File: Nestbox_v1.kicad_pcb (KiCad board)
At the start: 2 copper layers, 78 parts, among them P1 RX/TX, P2 TST/RST, P3 VDD/GND, P4 NFC_PWR_SEL, Q1 SFH 3605, SW1 SMD-BUTTON_2P-3.0X2.5X1.2+0.4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, U1 MSP430FR5969, U2 CR95HF, U3 TPS630250RNC, Y1 Crystal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

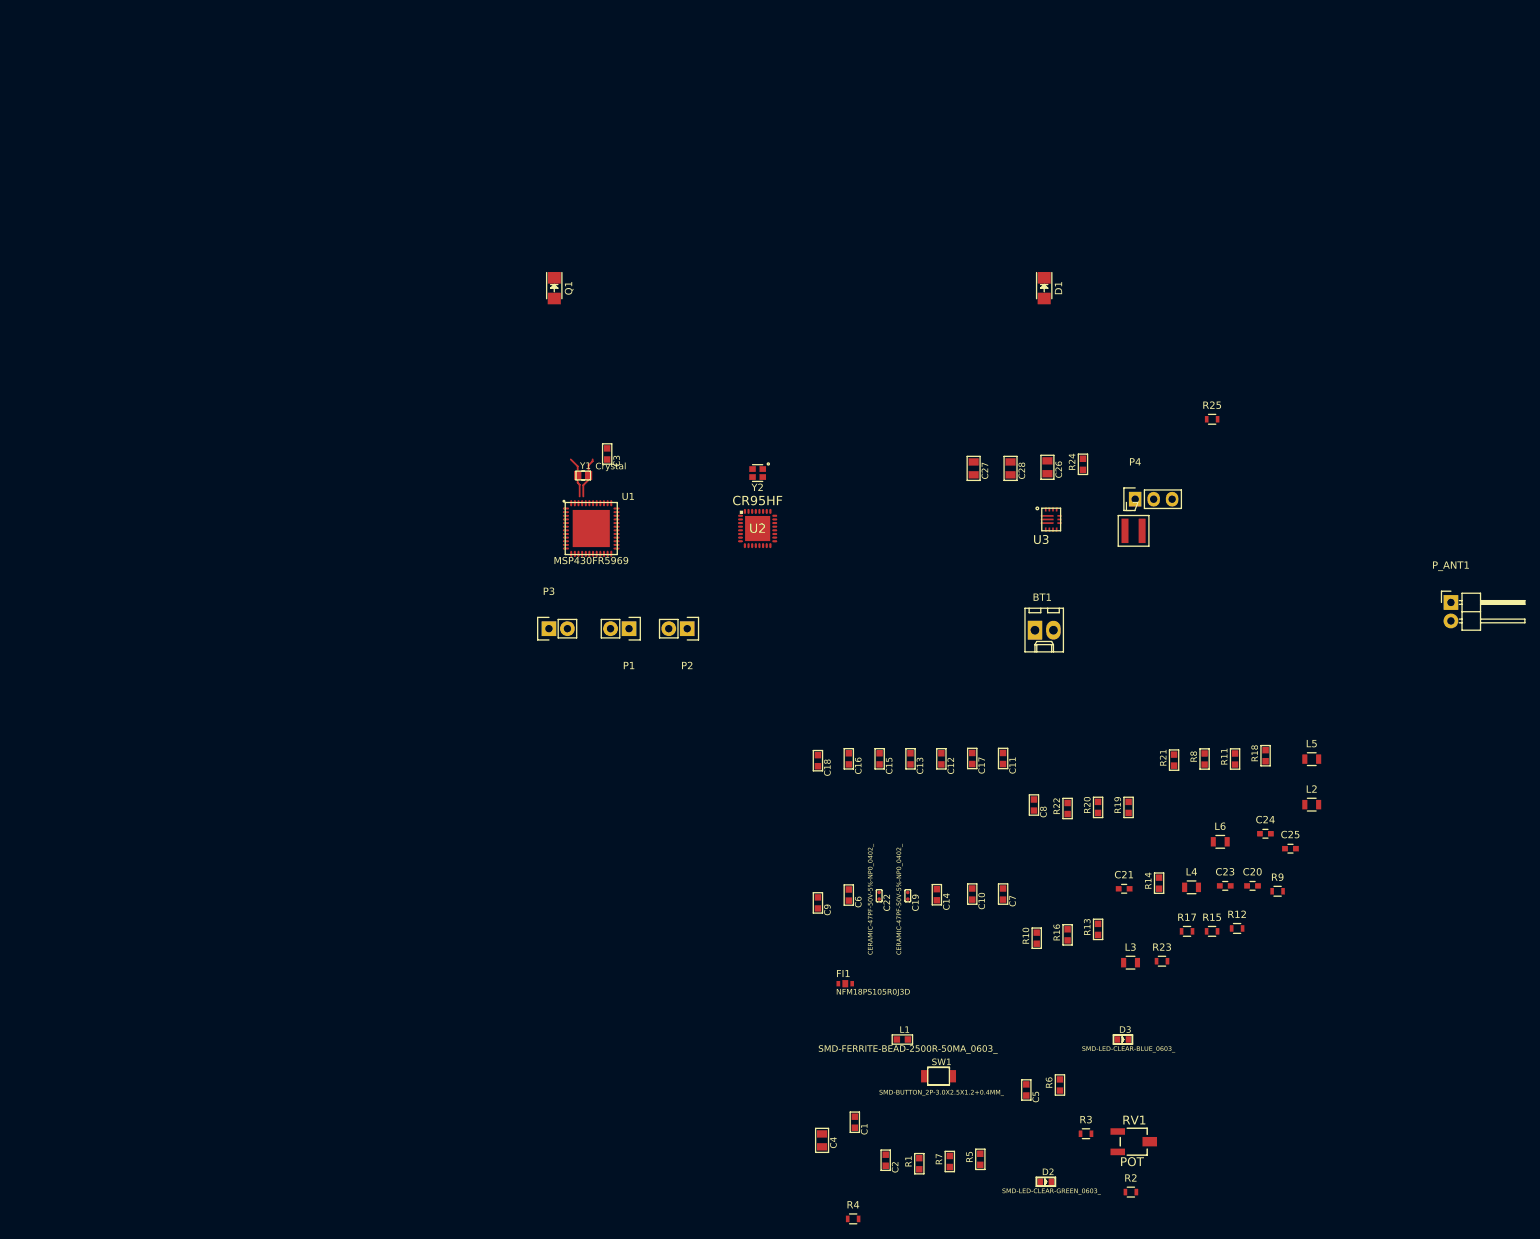
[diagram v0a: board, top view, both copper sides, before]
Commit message: pcb file components clustering
pcb file components were clustered according to the Eeschema -
currently everything is on one layer, F.Cu
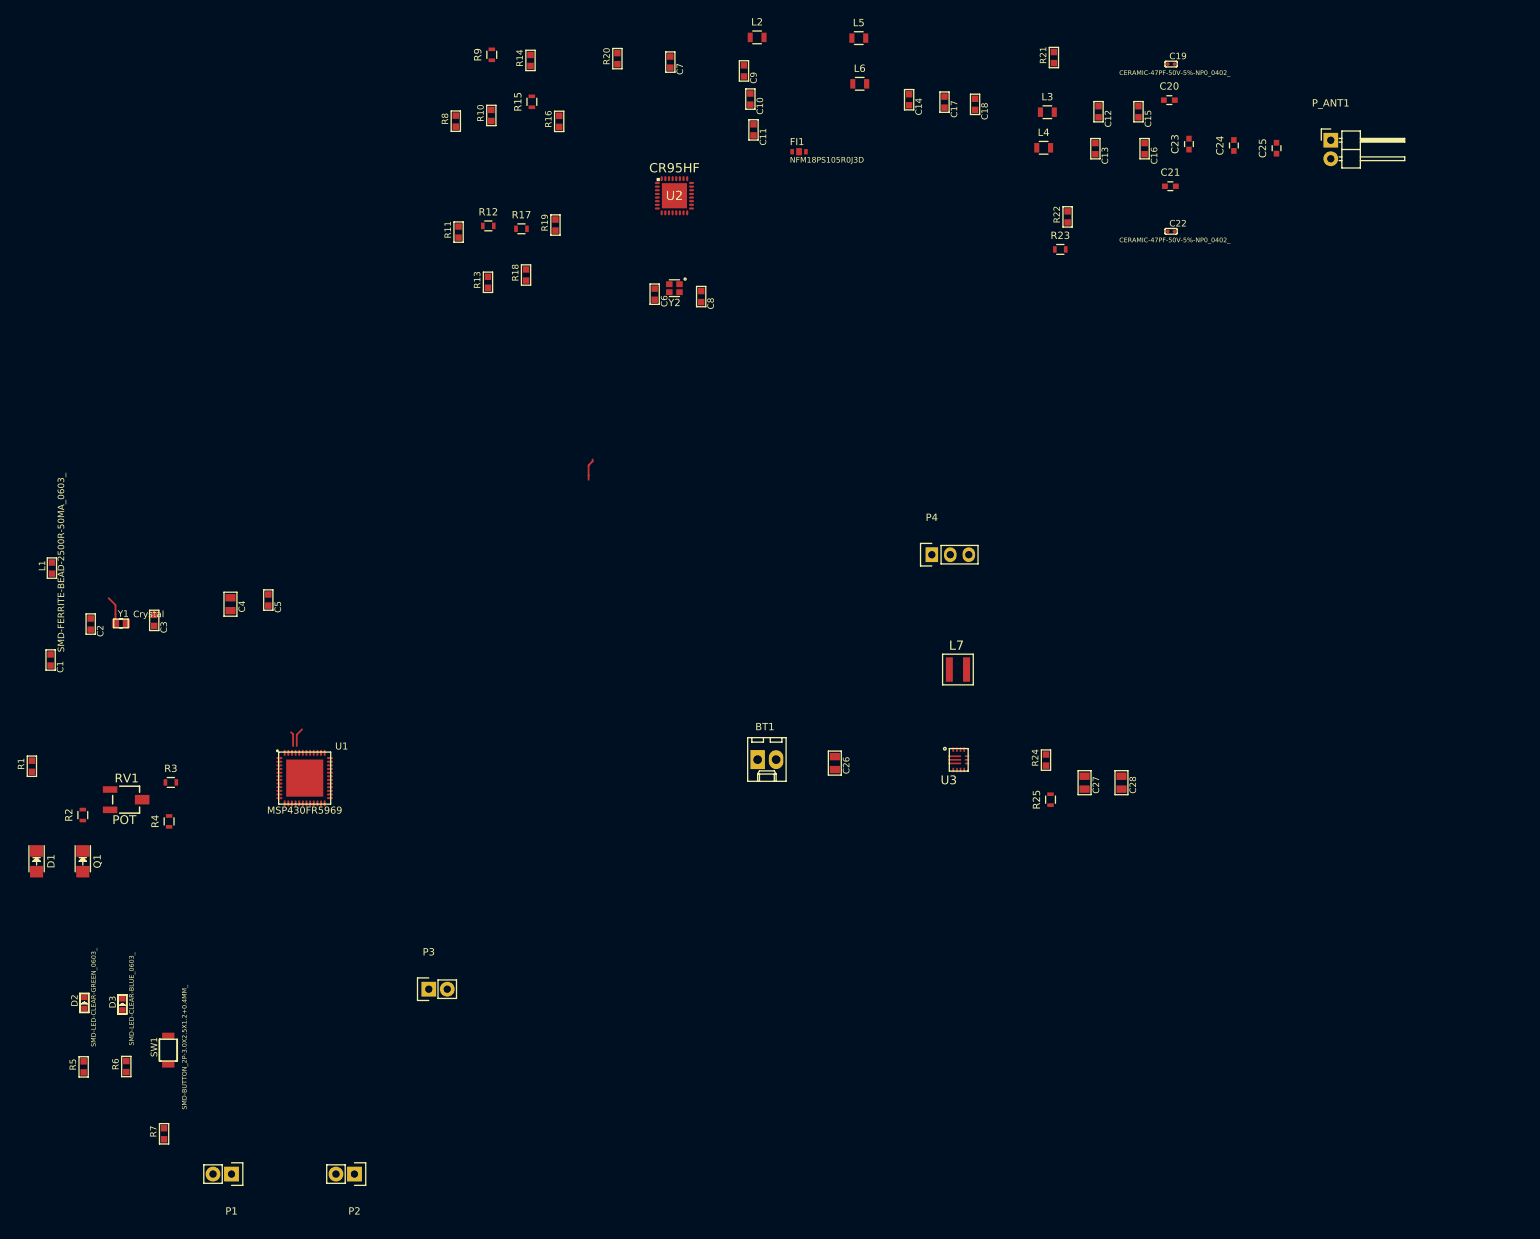
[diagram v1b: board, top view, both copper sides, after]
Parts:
- moved D1 159.3 mm to (64.6, 130.0)
- moved R9 157.7 mm to (127.1, 19.2), turned to 90 degrees
- moved R2 153.0 mm to (71.0, 123.6), turned to 90 degrees
- moved R15 147.4 mm to (132.7, 25.6), turned to 90 degrees
- moved RV1 146.2 mm to (76.9, 121.5)
- moved R14 142.2 mm to (132.5, 19.9)
- moved R12 141.1 mm to (126.7, 42.7)
- moved D3 137.5 mm to (76.4, 149.6), turned to 90 degrees
- moved R10 135.6 mm to (127.1, 27.5)
- moved R8 135.1 mm to (122.2, 28.3)
- moved R3 134.7 mm to (83.1, 119.1)
- moved D2 134.4 mm to (71.2, 149.4), turned to 90 degrees
- moved L1 133.6 mm to (66.7, 89.7), turned to 90 degrees
- moved R1 133.6 mm to (64.0, 116.9)
- moved R17 133.0 mm to (131.2, 43.1)
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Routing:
- net (no net): track 0.00 -> 7.61 mm
- net Net-(C3-Pad1): track 5.62 -> 0.00 mm
- net Net-(C2-Pad1): track 5.59 -> 3.59 mm

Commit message: circular NFC antenna added to pcb file, as well as other important changes and additions of library components
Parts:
- removed P_ANT1: CONN_01X02, Pin_Headers:Pin_Header_Angled_1x02
- added ant1: NFC_antenna, Octanis3:NFC_ANTENNA_CIRC, F.Cu at (242.4, 32.2)
- C4: value CERAMIC-10UF-10V-_-20%~+80%_-Y5V_0805_ -> CERAMIC-10UF-25V-10%-X5R_0805_
- moved C4 131.5 mm to (0.00, 0.00)
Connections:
- U1 pad 12: (no net) -> Net-(U1-Pad12)
- U1 pad 13: (no net) -> Net-(U1-Pad13)
- U1 pad 14: (no net) -> Net-(U1-Pad14)
- U1 pad 15: (no net) -> Net-(U1-Pad15)
- U1 pad 19: (no net) -> Net-(U1-Pad19)
- U1 pad 2: (no net) -> Net-(U1-Pad2)
- U1 pad 24: (no net) -> LORA_RX
- U1 pad 25: (no net) -> LORA_TX
- U1 pad 28: (no net) -> Net-(U1-Pad28)
- U1 pad 3: (no net) -> Net-(U1-Pad3)
- U1 pad 33: (no net) -> Net-(U1-Pad33)
- U1 pad 34: (no net) -> Net-(U1-Pad34)
- U1 pad 35: (no net) -> Net-(U1-Pad35)
- U1 pad 38: (no net) -> Net-(U1-Pad38)
- U1 pad 39: (no net) -> Net-(U1-Pad39)
- U1 pad 4: (no net) -> Net-(U1-Pad4)
- U1 pad 40: (no net) -> Net-(U1-Pad40)
- U1 pad 42: (no net) -> Net-(U1-Pad42)
- U1 pad 43: (no net) -> Net-(U1-Pad43)
- U1 pad 5: (no net) -> Net-(U1-Pad5)
- U1 pad 6: (no net) -> Net-(U1-Pad6)
- U1 pad 7: (no net) -> Net-(U1-Pad7)
- U1 pad 8: (no net) -> Net-(U1-Pad8)
- U1 pad 9: (no net) -> Net-(U1-Pad9)
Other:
- board outline added: 23 x 90 mm

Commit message: corrected antenna pin orientation
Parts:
- moved C4 163.2 mm to (161.8, 21.4)
- moved R18 98.1 mm to (225.3, 19.5), turned to 180 degrees
- moved R17 95.1 mm to (223.4, 19.5), turned to 270 degrees
- moved R11 94.7 mm to (215.1, 23.3), turned to 180 degrees
- moved R13 91.9 mm to (213.2, 19.5), turned to 180 degrees
- moved R12 91.4 mm to (215.1, 19.5), turned to 270 degrees
- moved R19 89.6 mm to (223.4, 23.3), turned to 180 degrees
- moved C7 73.3 mm to (224.6, 27.1), turned to 180 degrees
- moved U2 69.5 mm to (221.5, 32.8), turned to 180 degrees
- moved L5 62.2 mm to (231.0, 48.7), turned to 90 degrees
- moved C9 58.4 mm to (220.2, 22.6), turned to 270 degrees
- moved C10 57.5 mm to (220.2, 24.6), turned to 270 degrees
- moved L6 57.3 mm to (231.0, 44.2), turned to 90 degrees
- moved C11 57.2 mm to (220.2, 26.5), turned to 270 degrees
- moved L2 56.7 mm to (220.2, 20.7)
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
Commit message: NFC & power placed
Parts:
- moved P1 231.6 mm to (213.8, -23.7)
- moved P2 225.2 mm to (221.5, -21.8)
- moved D1 200.4 mm to (174.5, -37.7)
- moved Q1 200.4 mm to (180.8, -37.7)
- moved R1 200.4 mm to (173.8, -50.7)
- moved R6 200.4 mm to (186.8, -9.49)
- moved R7 200.4 mm to (192.0, -0.25)
- moved SW1 200.4 mm to (192.6, -11.7)
- moved C1 200.4 mm to (176.4, -65.3)
- moved C2 200.4 mm to (181.9, -70.3)
- moved C3 200.4 mm to (190.6, -70.8)
- moved C5 200.4 mm to (206.3, -73.6)
- moved D2 200.4 mm to (181.0, -18.2)
- moved D3 200.4 mm to (186.3, -18.0)
- moved L1 200.4 mm to (176.6, -78.0)
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
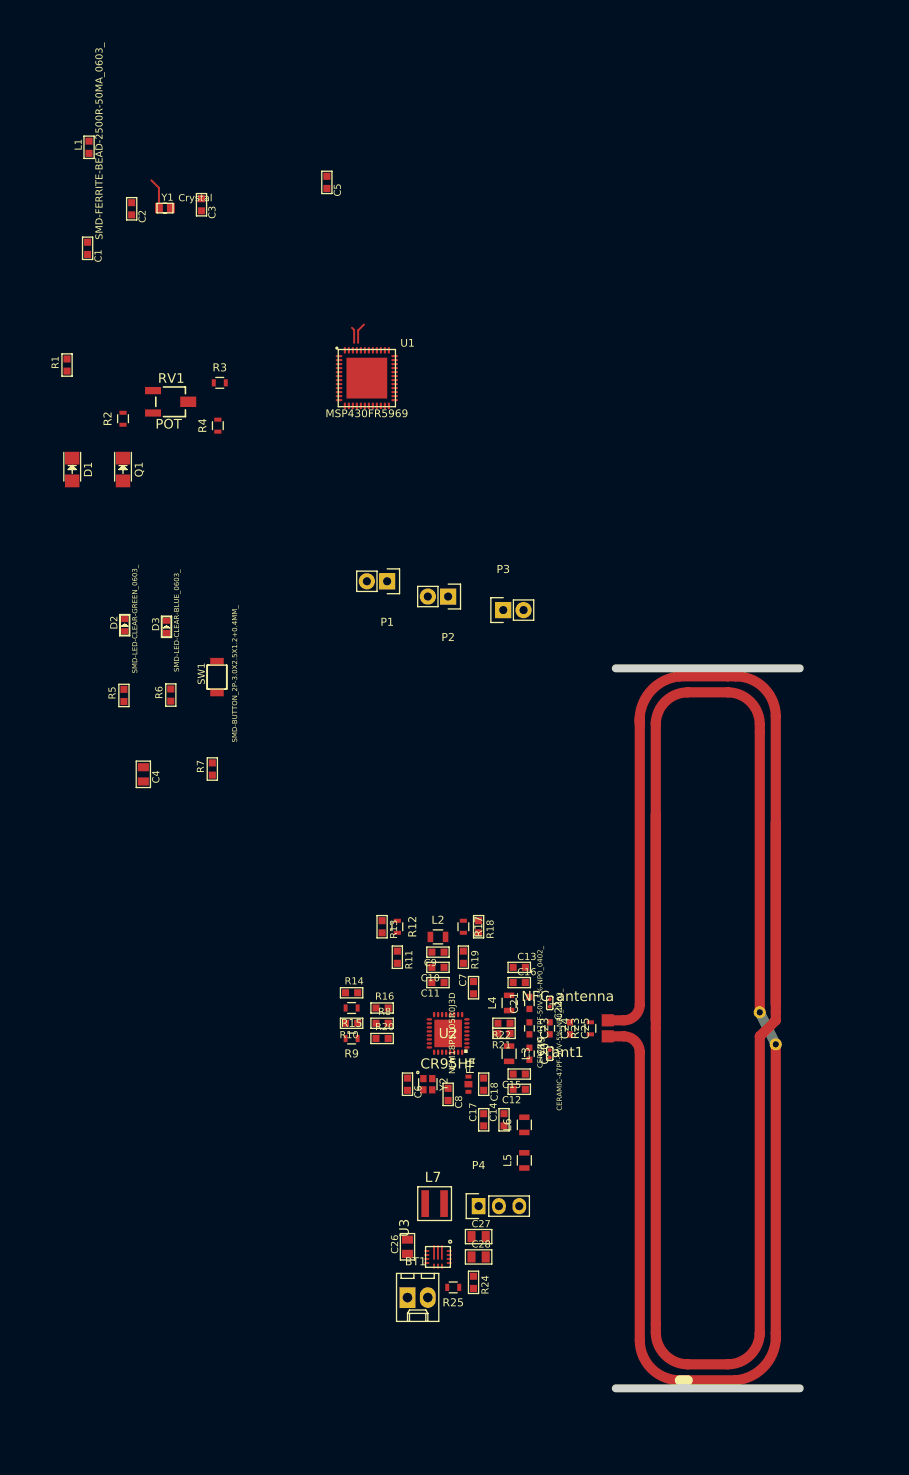
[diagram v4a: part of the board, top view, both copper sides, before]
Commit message: added lora component
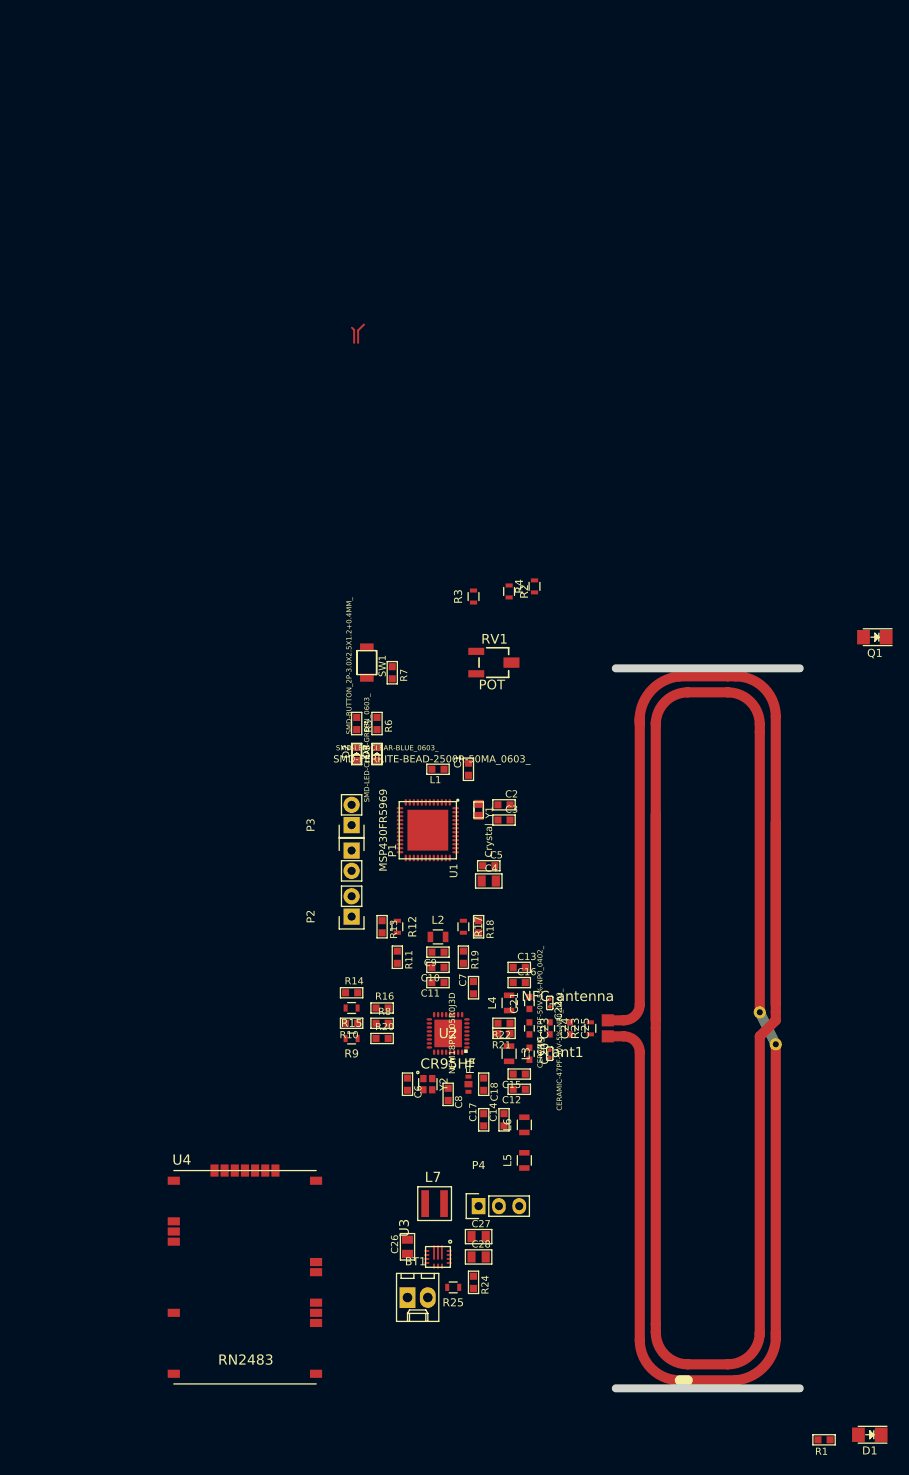
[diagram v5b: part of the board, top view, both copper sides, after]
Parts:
- added U4: RN2483, Octanis3:RN2483, F.Cu at (187.2, 76.6)
- R25: value R -> 180k
- moved R1 164.3 mm to (268.4, 83.6), turned to 90 degrees
- moved D1 156.5 mm to (274.2, 83.0), turned to 180 degrees
- moved Q1 96.3 mm to (274.8, -16.7), turned to 180 degrees
- moved L1 89.1 mm to (220.2, -0.21), turned to 180 degrees
- moved C2 87.8 mm to (228.4, 4.23), turned to 90 degrees
- moved C5 87.8 mm to (226.5, 11.8), turned to 90 degrees
- moved C3 85.7 mm to (228.4, 6.13), turned to 90 degrees
- moved Y1 84.8 mm to (225.3, 4.87), turned to 270 degrees
- moved C1 80.7 mm to (224.0, -0.21), turned to 180 degrees
- moved U1 57.0 mm to (218.9, 7.41), turned to 270 degrees
- moved R2 52.9 mm to (229.1, -22.4), turned to 270 degrees
- moved RV1 51.9 mm to (227.2, -13.6)
- moved C4 45.2 mm to (226.5, 13.8), turned to 90 degrees
- moved R4 44.4 mm to (232.2, -23.1)
- moved P2 41.8 mm to (209.4, 18.2), turned to 90 degrees
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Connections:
- U1 pad 12: Net-(U1-Pad12) -> (no net)
- U1 pad 13: Net-(U1-Pad13) -> (no net)
- U1 pad 14: Net-(U1-Pad14) -> (no net)
- U1 pad 15: Net-(U1-Pad15) -> (no net)
- U1 pad 19: Net-(U1-Pad19) -> (no net)
- U1 pad 2: Net-(U1-Pad2) -> (no net)
- U1 pad 28: Net-(U1-Pad28) -> (no net)
- U1 pad 3: Net-(U1-Pad3) -> (no net)
- U1 pad 33: Net-(U1-Pad33) -> (no net)
- U1 pad 34: Net-(U1-Pad34) -> (no net)
- U1 pad 35: Net-(U1-Pad35) -> (no net)
- U1 pad 38: Net-(U1-Pad38) -> (no net)
- U1 pad 39: Net-(U1-Pad39) -> (no net)
- U1 pad 4: Net-(U1-Pad4) -> (no net)
- U1 pad 40: Net-(U1-Pad40) -> (no net)
- U1 pad 42: Net-(U1-Pad42) -> (no net)
- U1 pad 43: Net-(U1-Pad43) -> (no net)
- U1 pad 5: Net-(U1-Pad5) -> (no net)
- U1 pad 6: Net-(U1-Pad6) -> (no net)
- U1 pad 7: Net-(U1-Pad7) -> (no net)
- U1 pad 8: Net-(U1-Pad8) -> (no net)
- U1 pad 9: Net-(U1-Pad9) -> (no net)
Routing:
- net Net-(C2-Pad1): track 3.59 -> 0.00 mm
